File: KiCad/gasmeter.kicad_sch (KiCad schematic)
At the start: 5 parts

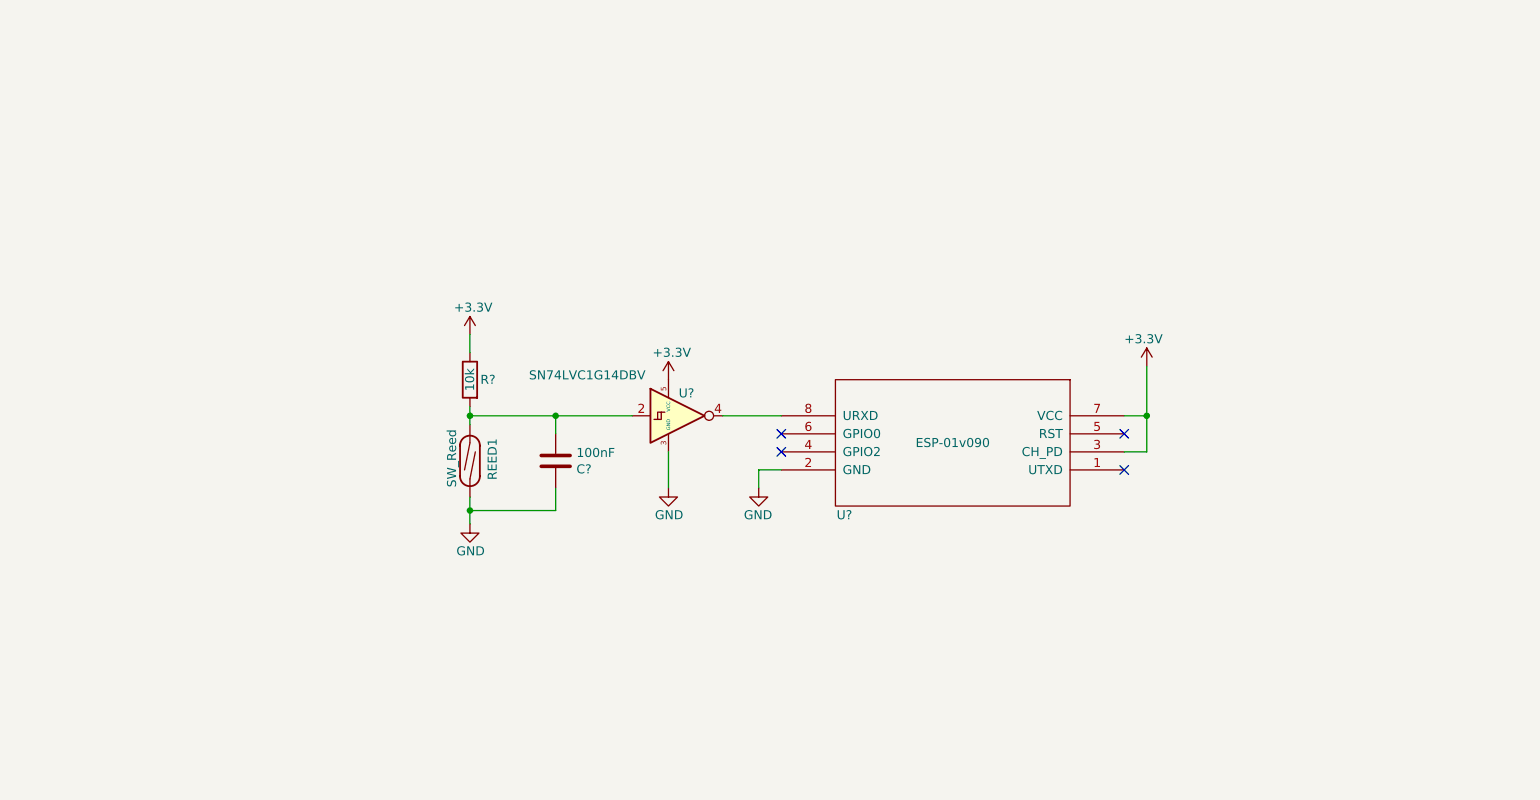
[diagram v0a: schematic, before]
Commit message: Cleaned up Schematic Layout
Layout Cleanup, Added DC Input and protection. Now runs with 5V input.
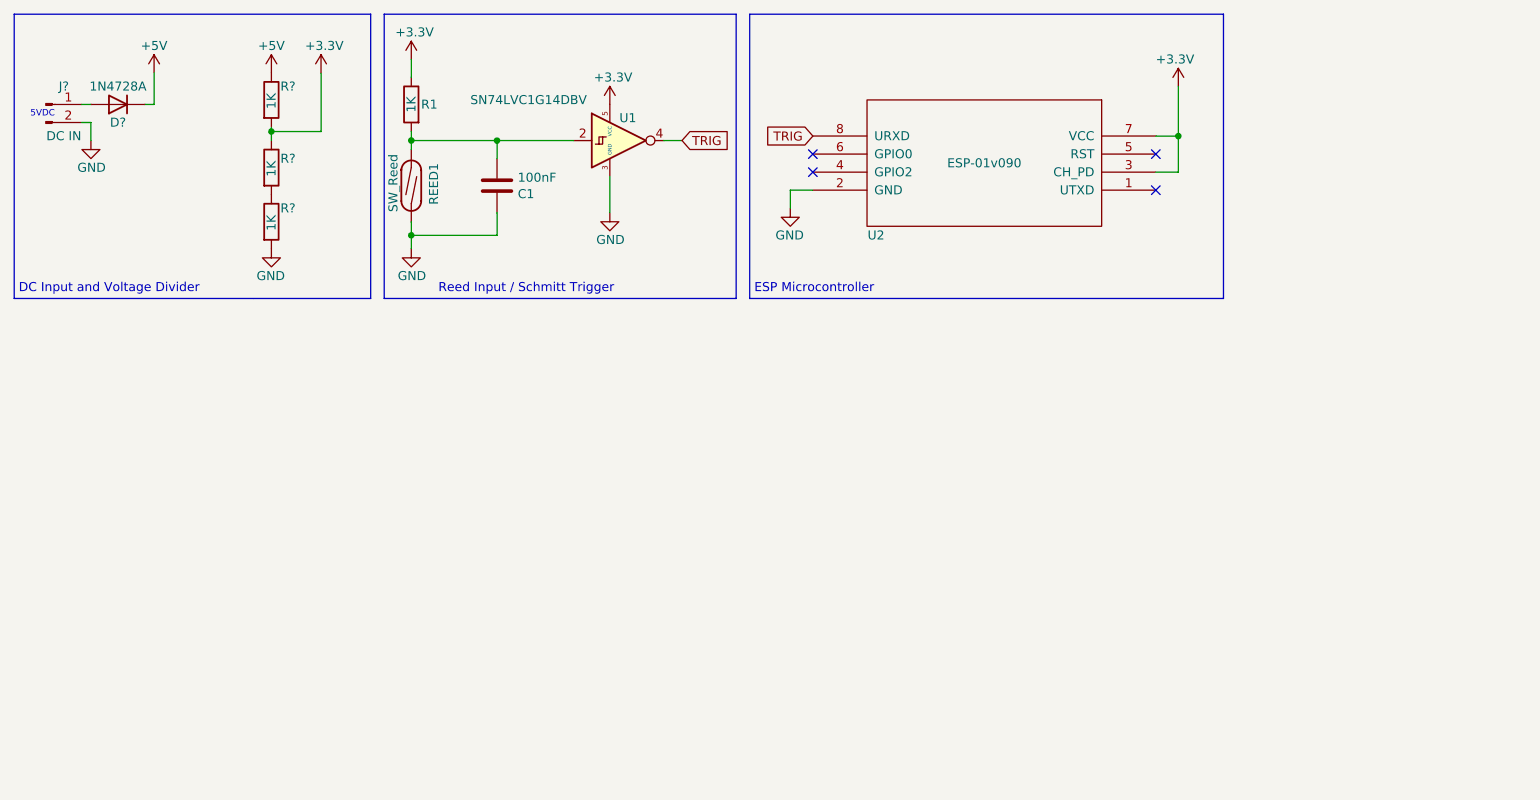
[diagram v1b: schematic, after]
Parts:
- added D?: 1N4728A, symbol Device:D
- added J?: DC IN, symbol Connector:Conn_01x02_Male
- added R? (x3): 1K, symbol Device:R
- R1: renamed from R?; value 10k -> 1K
- REED1: footprint Button_Switch_SMD:SW_SPST_REED_CT10-XXXX-G4 -> Connector_JST:JST_PH_B2B-PH-K_1x02_P2.00mm_Vertical
- U2: renamed from U?; footprint (none) -> Connector_PinHeader_2.54mm:PinHeader_2x04_P2.54mm_Vertical
- gave numbers to parts that had none: 2
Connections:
- net +3V3: now also R?.1, R?.2
- net GND: now also J?.2 (Pin_2), R?.2
- net TRIG: now reaches U1.4, U2.8 (URXD)
- new net: D?.2 (A), J?.1 (Pin_1)
- new net: R?.1, R?.2
- new net +5V: D?.1 (K), R?.1
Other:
- note added: "5VDC"
- note added: "DC Input and Voltage Divider"
- note added: "ESP Microcontroller"
- note added: "Reed Input / Schmitt Trigger"
- moved on the sheet: C1, R1, REED1, U1, U2

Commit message: Refactored Design
* Now runs using an ESP12E
* LED Indicators added
* Programming Header
* Optional USB UART interface onboard
* USB-C Power/Data (power-only if UART not populated)
* Diode-based Voltage Divider
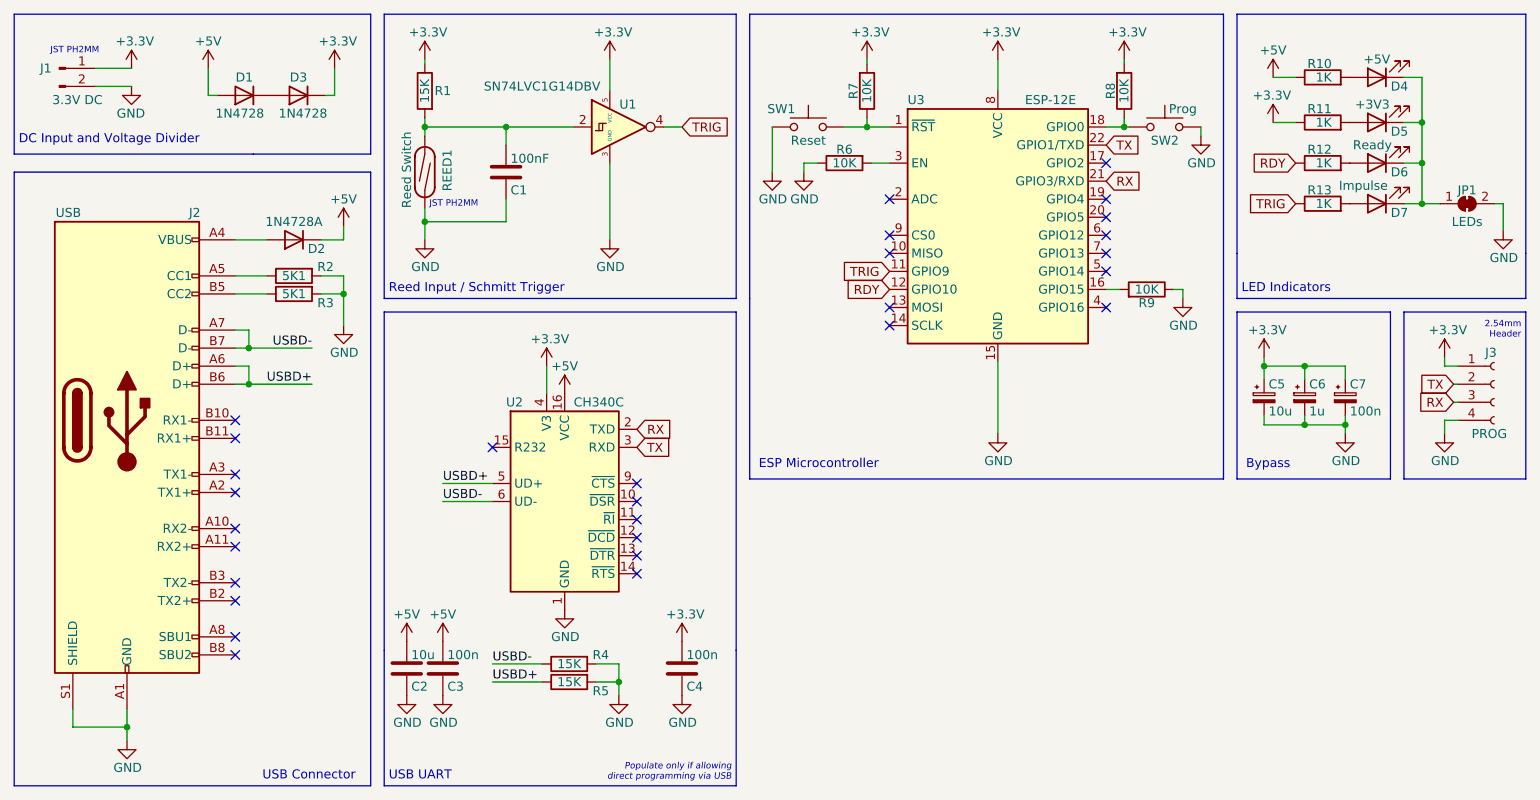
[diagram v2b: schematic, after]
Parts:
- removed J?: DC IN, symbol Connector:Conn_01x02_Male
- removed R? (x3): 1K, symbol Device:R
- removed U2: ESP-01v090, Connector_PinHeader_2.54mm:PinHeader_2x04_P2.54mm_Vertical, symbol ESP8266:ESP-01v090
- added C2: 10u, Capacitor_SMD:C_0805_2012Metric_Pad1.18x1.45mm_HandSolder, symbol Device:C
- added C3, C4: 100n, Capacitor_SMD:C_0805_2012Metric_Pad1.18x1.45mm_HandSolder, symbol Device:C
- added C5: 10u, Capacitor_SMD:C_0805_2012Metric_Pad1.18x1.45mm_HandSolder, symbol Device:C_Polarized_Small
- added C6: 1u, Capacitor_SMD:C_0805_2012Metric_Pad1.18x1.45mm_HandSolder, symbol Device:C_Polarized_Small
- added C7: 100n, Capacitor_SMD:C_0805_2012Metric_Pad1.18x1.45mm_HandSolder, symbol Device:C_Polarized_Small
- added D1, D3: 1N4728, Diode_SMD:D_0805_2012Metric_Pad1.15x1.40mm_HandSolder, symbol Device:D
- added D4: +5V, LED_SMD:LED_0805_2012Metric_Pad1.15x1.40mm_HandSolder, symbol Device:LED
- added D5: +3V3, LED_SMD:LED_0805_2012Metric_Pad1.15x1.40mm_HandSolder, symbol Device:LED
- added D6: Ready, LED_SMD:LED_0805_2012Metric_Pad1.15x1.40mm_HandSolder, symbol Device:LED
- added D7: Impulse, LED_SMD:LED_0805_2012Metric_Pad1.15x1.40mm_HandSolder, symbol Device:LED
- added J1: 3.3V DC, Connector_JST:JST_PH_B2B-PH-K_1x02_P2.00mm_Vertical, symbol Connector:Conn_01x02_Male
- added J2: USB, Connector_USB:USB_C_Receptacle_Amphenol_12401548E4-2A, symbol Connector:USB_C_Receptacle
- added J3: PROG, Connector_PinHeader_2.54mm:PinHeader_1x04_P2.54mm_Vertical, symbol Connector:Conn_01x04_Female
- added JP1: LEDs, Jumper:SolderJumper-2_P1.3mm_Bridged_Pad1.0x1.5mm, symbol Jumper:SolderJumper_2_Bridged
- added R10, R11, R12, R13: 1K, Resistor_SMD:R_0805_2012Metric_Pad1.20x1.40mm_HandSolder, symbol Device:R
- added R2, R3: 5K1, Resistor_SMD:R_0805_2012Metric_Pad1.20x1.40mm_HandSolder, symbol Device:R
- added R4, R5: 15K, Resistor_SMD:R_0805_2012Metric_Pad1.20x1.40mm_HandSolder, symbol Device:R
- added R6, R7, R8, R9: 10K, Resistor_SMD:R_0805_2012Metric_Pad1.20x1.40mm_HandSolder, symbol Device:R
- added SW1: Reset, Button_Switch_SMD:SW_SPST_EVQP2, symbol Switch:SW_Push
- added SW2: Prog, Button_Switch_SMD:SW_SPST_EVQP2, symbol Switch:SW_Push
- added U2: CH340C, Package_SO:SOIC-16_3.9x9.9mm_P1.27mm, symbol Interface_USB:CH340C
- added U3: ESP-12E, RF_Module:ESP-12E, symbol RF_Module:ESP-12E
- D2: renamed from D?; footprint (none) -> Diode_SMD:D_0805_2012Metric_Pad1.15x1.40mm_HandSolder
- R1: value 1K -> 15K
- REED1: value SW_Reed -> Reed Switch
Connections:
- net +3V3: now also C4.2, C5.1, C6.1, C7.1, D3.1 (K), J1.1 (Pin_1), J3.1 (Pin_1), R11.1, R7.2, R8.2, U2.4 (V3), U3.8 (VCC)
- net +5V: now also C2.2, C3.2, D1.2 (A), R10.1, U2.16 (VCC)
- net GND: now also C2.1, C3.1, C4.1, C5.2, C6.2, C7.2, J1.2 (Pin_2), J2.A1 (GND), J2.A12 (GND), J2.B1 (GND), J2.B12 (GND), J2.S1 (SHIELD), J3.4 (Pin_4), JP1.2 (B), R2.2, R3.2, R4.2, R5.2, R6.1, R9.1, SW1.1, SW2.2, U2.1 (GND), U3.15 (GND)
- net TRIG: now also R13.1, U3.11 (GPIO9)
- net at D2.2 (A): now also J2.A4 (VBUS), J2.A9 (VBUS), J2.B4 (VBUS), J2.B9 (VBUS)
- new net: D4.1 (K), D5.1 (K), D6.1 (K), D7.1 (K), JP1.1 (A)
- new net: R9.2, U3.16 (GPIO15)
- new net: D6.2 (A), R12.2
- new net: D5.2 (A), R11.2
- new net: J2.A5 (CC1), R2.1
- new net: J2.B5 (CC2), R3.1
- new net: D7.2 (A), R13.2
- new net: D1.1 (K), D3.2 (A)
- new net: R7.1, SW1.2, U3.1 (~{RST})
- new net: R8.1, SW2.1, U3.18 (GPIO0)
- new net: R6.2, U3.3 (EN)
- new net: D4.2 (A), R10.2
- new net RDY: R12.1, U3.12 (GPIO10)
- new net RX: J3.3 (Pin_3), U2.2 (TXD), U3.21 (GPIO3/RXD)
- new net TX: J3.2 (Pin_2), U2.3 (RXD), U3.22 (GPIO1/TXD)
- new net USBD+: J2.A6 (D+), J2.B6 (D+), R5.1, U2.5 (UD+)
- new net USBD-: J2.A7 (D-), J2.B7 (D-), R4.1, U2.6 (UD-)
- no-connect marks 4 -> 29
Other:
- note added: "2.54mm Header"
- note added: "Bypass"
- note added: "JST PH2MM"
- note added: "LED Indicators"
- note added: "Populate only if allowing direct programming via USB"
- note added: "USB Connector"
- note added: "USB UART"
- note removed: "5VDC"
- moved on the sheet: C1, D2, R1, REED1, U1
